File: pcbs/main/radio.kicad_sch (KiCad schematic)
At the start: 1 part, among them J11 nrf24l01

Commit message: fea: add jumpers to I2C encoders config
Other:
- title: (none) -> SSL main board
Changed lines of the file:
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@@
 	(generator_version "9.0")
 	(paper "A4")
+	(title_block
+		(title "SSL main board")
+	)
 	(wire
 		(pts

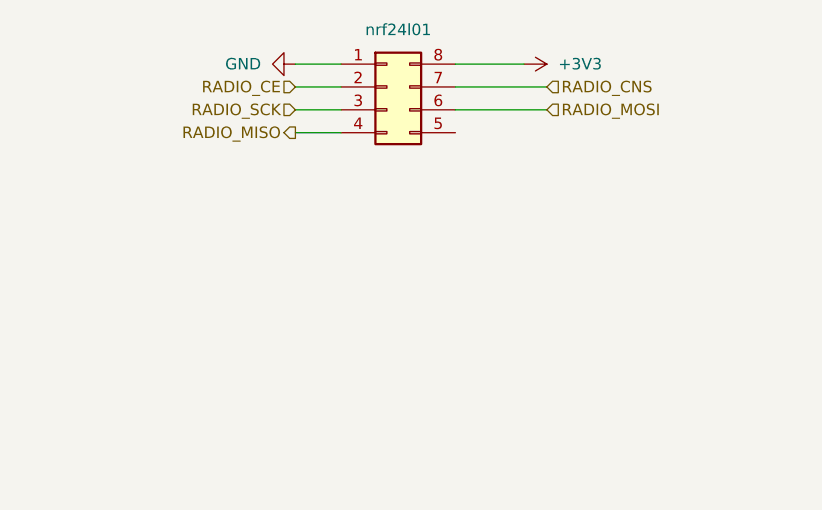
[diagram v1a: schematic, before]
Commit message: wip: change radio footprint
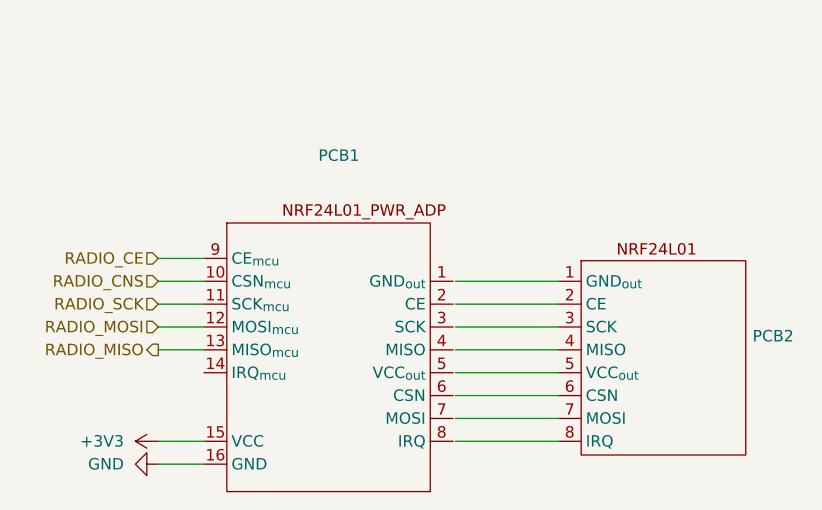
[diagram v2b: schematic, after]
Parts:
- removed J11: nrf24l01, symbol Connector_Generic:Conn_02x04_Counter_Clockwise
- added PCB1: ~, symbol oxebots:NRF24L01_PWR_ADP
- added PCB2: ~, symbol oxebots:NRF24L01
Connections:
- net +3V3: now also PCB1.15 (VCC)
- net GND: now also PCB1.16 (GND)
- net RADIO_CE: now also PCB1.9 (CE_{mcu})
- net RADIO_CNS: now also PCB1.10 (CSN_{mcu})
- net RADIO_MISO: now also PCB1.13 (MISO_{mcu})
- net RADIO_MOSI: now also PCB1.12 (MOSI_{mcu})
- net RADIO_SCK: now also PCB1.11 (SCK_{mcu})

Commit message: feat: association of footprints
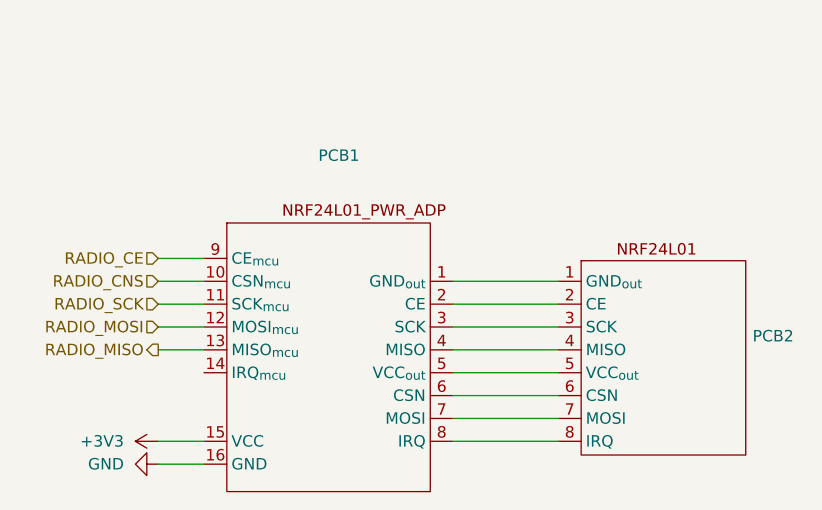
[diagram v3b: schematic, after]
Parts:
- PCB1: footprint (none) -> Oxebots Footprints:NRF24L01_PWR_ADP
- PCB2: footprint (none) -> Oxebots Footprints:NRF24L01
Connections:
- net at PCB2.1 (GND_{out}): now also PCB1.1 (GND_{out})
- net at PCB2.2 (CE): now also PCB1.2 (CE)
- net at PCB2.3 (SCK): now also PCB1.3 (SCK)
- net at PCB2.4 (MISO): now also PCB1.4 (MISO)
- net at PCB2.5 (VCC_{out}): now also PCB1.5 (VCC_{out})
- net at PCB2.6 (CSN): now also PCB1.6 (CSN)
- net at PCB2.7 (MOSI): now also PCB1.7 (MOSI)
- net at PCB2.8 (IRQ): now also PCB1.8 (IRQ)
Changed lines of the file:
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@@
 	(wire
 		(pts
-			(xy 132.08 118.11) (xy 143.51 118.11)
-		)
-		(stroke
-			(width 0)
-			(type default)
-		)
-	)
-	(wire
-		(pts
-			(xy 132.08 123.19) (xy 143.51 123.19)
+			(xy 131.8259 113.03) (xy 143.51 113.03)
 		)
 		(stroke
@@
 	(wire
 		(pts
+			(xy 131.8259 128.27) (xy 143.51 128.27)
+		)
+		(stroke
+			(width 0)
+			(type default)
+		)
+	)
+	(wire
+		(pts
 			(xy 99.06 107.95) (xy 104.14 107.95)
 		)
@@
 	(wire
 		(pts
+			(xy 131.8259 115.57) (xy 143.51 115.57)
+		)
+		(stroke
+			(width 0)
+			(type default)
+		)
+	)
+	(wire
+		(pts
 			(xy 99.06 113.03) (xy 104.14 113.03)
 		)
@@
 	(wire
 		(pts
+			(xy 131.8259 110.49) (xy 143.51 110.49)
+		)
+		(stroke
+			(width 0)
+			(type default)
+		)
+	)
+	(wire
+		(pts
 			(xy 99.06 115.57) (xy 104.14 115.57)
 		)
@@
 	(wire
 		(pts
-			(xy 132.08 128.27) (xy 143.51 128.27)
-		)
-		(stroke
-			(width 0)
-			(type default)
-		)
-	)
-	(wire
-		(pts
-			(xy 132.08 110.49) (xy 143.51 110.49)
-		)
-		(stroke
-			(width 0)
-			(type default)
-		)
-	)
-	(wire
-		(pts
-			(xy 132.08 115.57) (xy 143.51 115.57)
-		)
-		(stroke
-			(width 0)
-			(type default)
-		)
-	)
-	(wire
-		(pts
-			(xy 132.08 125.73) (xy 143.51 125.73)
-		)
-		(stroke
-			(width 0)
-			(type default)
-		)
-	)
-	(wire
-		(pts
 			(xy 99.06 130.81) (xy 104.14 130.81)
 		)
@@
 	(wire
 		(pts
+			(xy 131.8259 118.11) (xy 143.51 118.11)
+		)
+		(stroke
+			(width 0)
+			(type default)
+		)
+	)
+	(wire
+		(pts
+			(xy 131.8259 120.65) (xy 143.51 120.65)
+		)
+		(stroke
+			(width 0)
+			(type default)
+		)
+	)
+	(wire
+		(pts
+			(xy 131.8259 125.73) (xy 143.51 125.73)
+		)
+		(stroke
+			(width 0)
+			(type default)
+		)
+	)
+	(wire
+		(pts
 			(xy 99.06 110.49) (xy 104.14 110.49)
 		)
@@
 	(wire
 		(pts
-			(xy 132.08 120.65) (xy 143.51 120.65)
-		)
-		(stroke
-			(width 0)
-			(type default)
-		)
-	)
-	(wire
-		(pts
-			(xy 132.08 113.03) (xy 143.51 113.03)
+			(xy 131.8259 123.19) (xy 143.51 123.19)
 		)
 		(stroke
@@
 			)
 		)
-		(property "Footprint" ""
+		(property "Footprint" "Oxebots Footprints:NRF24L01"
 			(at 156.21 118.11 0)
 			(effects
@@
 			)
 		)
-		(property "Footprint" ""
+		(property "Footprint" "Oxebots Footprints:NRF24L01_PWR_ADP"
 			(at 118.11 119.38 0)
 			(effects
